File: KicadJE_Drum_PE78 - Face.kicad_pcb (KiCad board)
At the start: 2 copper layers, 183 x 128 mm, 212 parts, among them J101 Snare, J102 LCymbals, J103 SCymbals, J104 Maracas, J105 Bass, J106 LBongo, J107 HBongo, J108 Claves, J201 AudioJack2_SwitchT, J202 AudioJack2_SwitchT, J203 AudioJack2_SwitchT, J204 Power +, J205 Power -, J206 Conn_01x03_Male, J207 Conn_01x03_Male, J208 Conn_01x03_Male, J209 Conn_01x03_Male, J210 Conn_01x02_Male, J301 Tone/Noise, J302 RND, J303 Noise, J304 DRUM_OUT, J401 Tone/Noise, P101 HEADER_2x8_Doepfer, P201 HEADER_2x5_Doepfer, P401 HEADER_2x8_Doepfer, Q101 2N3904, Q102 2N3904, Q103 2N3904, Q104 2N3904, SW201 SW_SPDT, U101 74HC04, U302 TL072

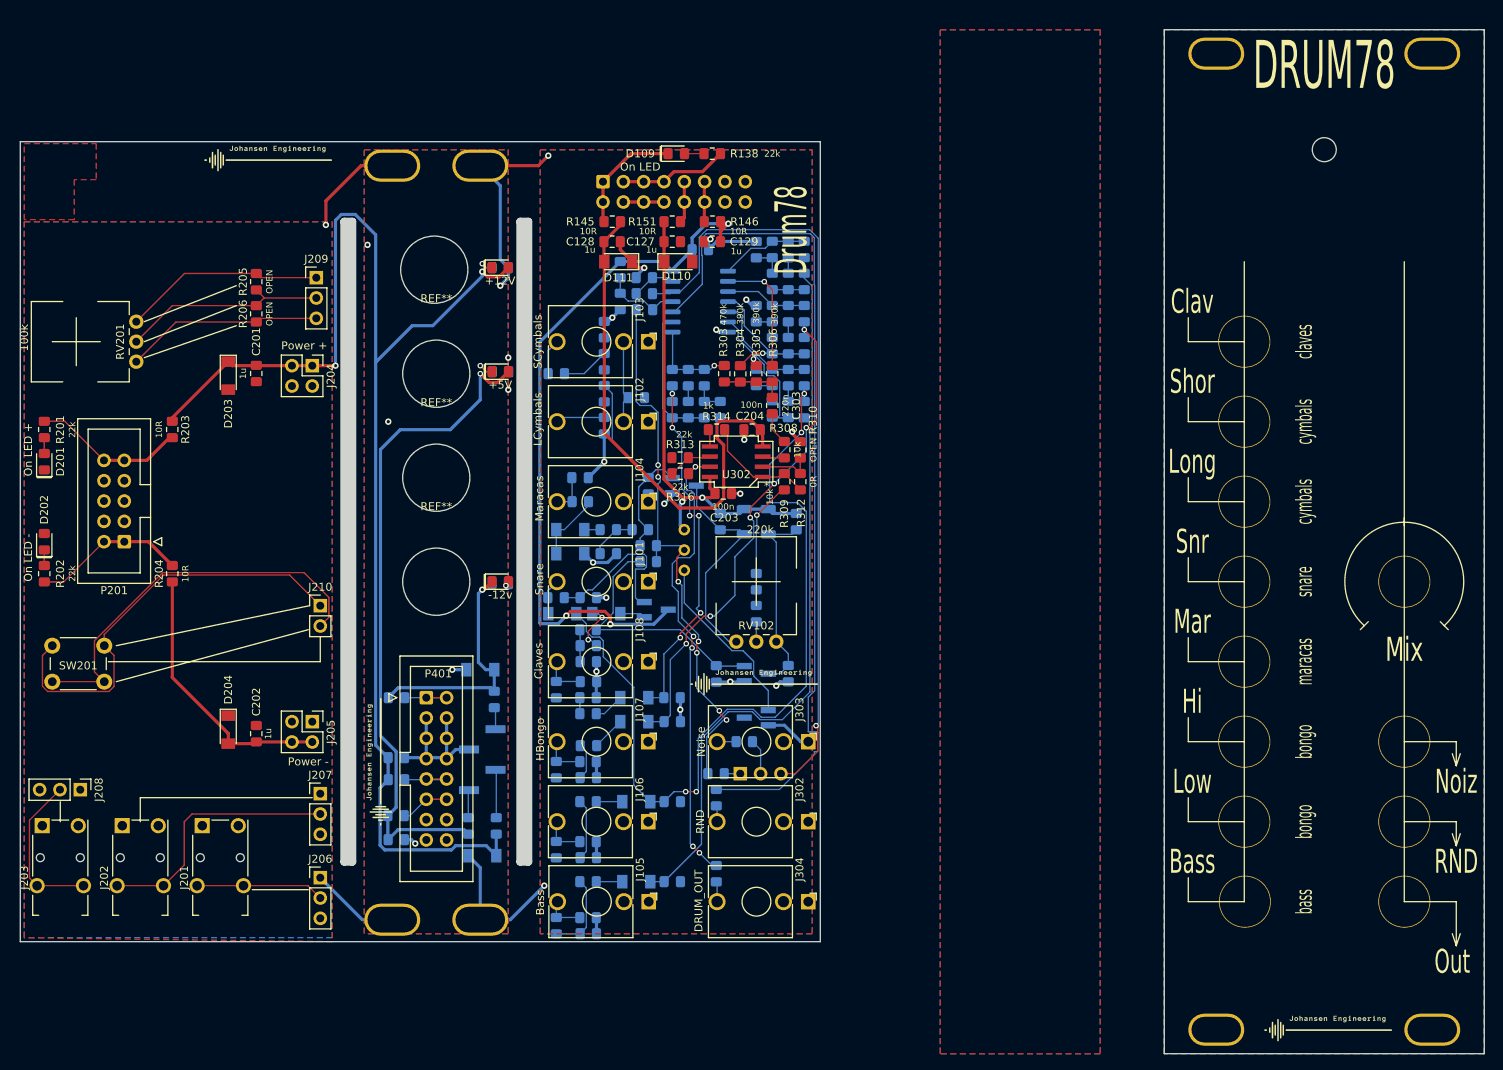
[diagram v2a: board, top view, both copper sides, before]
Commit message: base removed from face pcb
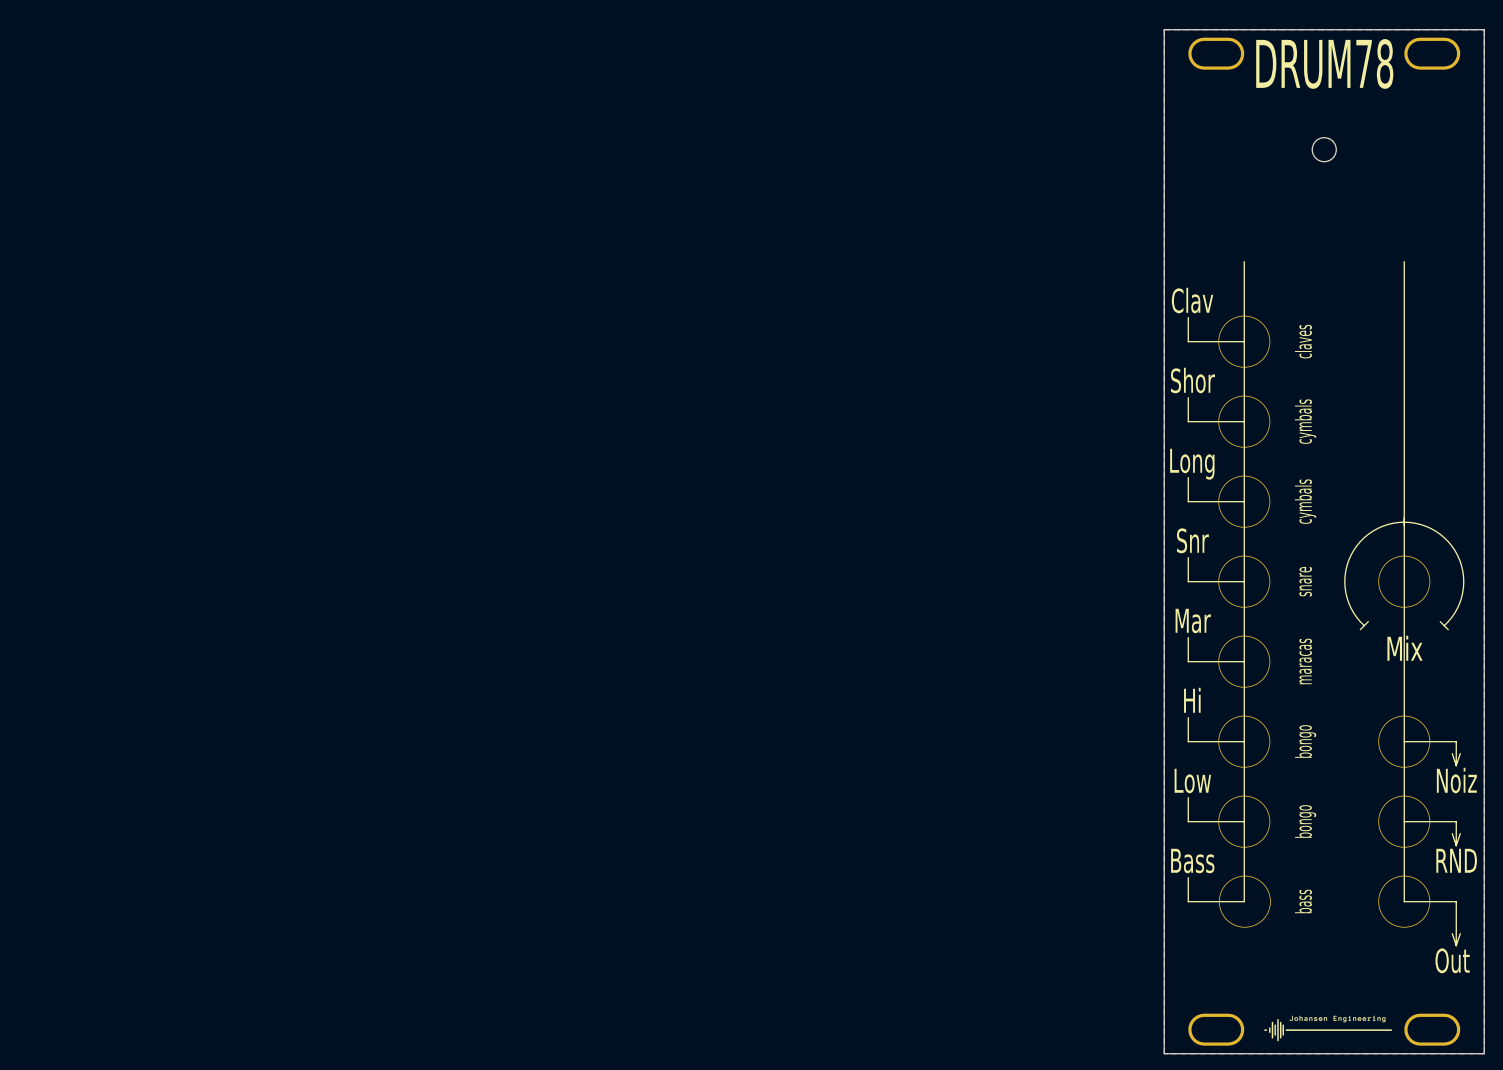
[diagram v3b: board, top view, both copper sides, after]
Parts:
- removed C101: 330n, AJ:C_0805_AJ
- removed C102, C107, C120, C130, C203, C204: 100n, AJ:C_0805_AJ
- removed C103, C303, C304: 220n, AJ:C_0805_AJ
- removed C104, C113: 150n, AJ:C_0805_AJ
- removed C105, C109, C114, C115: 47n, AJ:C_0805_AJ
- removed C106, C108: 68n, AJ:C_0805_AJ
- removed C110, C116: 15n, AJ:C_0805_AJ
- removed C111, C112, C119, C124, C301, C302: 4n7, AJ:C_0805_AJ
- removed C117: 22n, AJ:C_0805_AJ
- removed C118, C123: 33n, AJ:C_0805_AJ
- removed C121, C125: 10n, AJ:C_0805_AJ
- removed C122, C126: 1n5, AJ:C_0805_AJ
- removed C127, C128, C129, C201, C202, C401, C403: 1u, AJ:C_0805_AJ
- removed D101, D102, D103, D104, D105, D106, D107, D108: 1N4148, Diode_SMD:D_MiniMELF
- removed D109: On LED, AJ:D_0805_AJ
- removed D110, D111, D203, D204, D404, D405: 1N4007, Diode_SMD:D_MiniMELF
- removed D201: On LED +, AJ:D_0805_AJ
- removed D202: On LED -, AJ:D_0805_AJ
- removed D401: +12V, AJ:D_0805_AJ
- removed D402: +5V, AJ:D_0805_AJ
- removed D403: -12v, AJ:D_0805_AJ
- removed the G*** at (95.0, 127.5)
- removed the G*** at (141.8, 117.8)
- removed the G*** at (58.5, 52.2)
- removed the G*** at (87.5, 95.0)
- removed the G*** at (81.0, 52.2)
- removed the H103 at (107.5, 53.0)
- removed the H103 at (96.5, 53.0)
- removed the H103 at (107.5, 147.2)
- removed the H103 at (96.5, 147.2)
- removed J101: Snare, Connector_Audio:Jack_3.5mm_QingPu_WQP-PJ398SM_Vertical_CircularHoles
- removed J102: LCymbals, Connector_Audio:Jack_3.5mm_QingPu_WQP-PJ398SM_Vertical_CircularHoles
- removed J103: SCymbals, Connector_Audio:Jack_3.5mm_QingPu_WQP-PJ398SM_Vertical_CircularHoles
- removed J104: Maracas, Connector_Audio:Jack_3.5mm_QingPu_WQP-PJ398SM_Vertical_CircularHoles
- removed J105: Bass, Connector_Audio:Jack_3.5mm_QingPu_WQP-PJ398SM_Vertical_CircularHoles
- removed J106: LBongo, Connector_Audio:Jack_3.5mm_QingPu_WQP-PJ398SM_Vertical_CircularHoles
- removed J107: HBongo, Connector_Audio:Jack_3.5mm_QingPu_WQP-PJ398SM_Vertical_CircularHoles
- removed J108: Claves, Connector_Audio:Jack_3.5mm_QingPu_WQP-PJ398SM_Vertical_CircularHoles
- removed J201, J202, J203: AudioJack2_SwitchT, Connector_Audio:Jack_3.5mm_Switronic_ST-005-G_horizontal
- removed J204: Power +, Connector_PinHeader_2.54mm:PinHeader_2x02_P2.54mm_Vertical
- removed J205: Power -, Connector_PinHeader_2.54mm:PinHeader_2x02_P2.54mm_Vertical
- removed J206, J207, J208, J209: Conn_01x03_Male, Connector_PinHeader_2.54mm:PinHeader_1x03_P2.54mm_Vertical
- removed J210: Conn_01x02_Male, Connector_PinHeader_2.54mm:PinHeader_1x02_P2.54mm_Vertical
- removed J301: Tone/Noise, Connector_PinHeader_2.54mm:PinHeader_1x03_P2.54mm_Vertical
- removed J302: RND, Connector_Audio:Jack_3.5mm_QingPu_WQP-PJ398SM_Vertical_CircularHoles
- removed J303: Noise, Connector_Audio:Jack_3.5mm_QingPu_WQP-PJ398SM_Vertical_CircularHoles
- removed J304: DRUM_OUT, Connector_Audio:Jack_3.5mm_QingPu_WQP-PJ398SM_Vertical_CircularHoles
- removed J401: Tone/Noise, Connector_PinHeader_2.54mm:PinHeader_1x04_P2.54mm_Vertical_SMD_Pin1Left
- removed L103, L104: 100mH, Inductor_SMD:L_1206_3216Metric
- removed P101, P401: HEADER_2x8_Doepfer, Connector_IDC:IDC-Header_2x08_P2.54mm_Vertical
- removed P201: HEADER_2x5_Doepfer, Connector_IDC:IDC-Header_2x05_P2.54mm_Vertical
- removed Q101, Q102, Q103, Q104: 2N3904, Package_TO_SOT_SMD:SOT-23_Handsoldering
- removed R101, R103, R116, R117, R139, R140, R308, R309, R311, R405: 10k, AJ:R_0805_AJ
- removed R102, R106, R131, R138, R201, R202, R313, R316, R404, R406: 22k, AJ:R_0805_AJ
- removed R104, R105, R132, R133: 12k, AJ:R_0805_AJ
- removed R107, R108, R134, R135: 47k, AJ:R_0805_AJ
- removed R109, R110, R118, R123, R128: 1M, AJ:R_0805_AJ
- removed R111, R112, R136, R137: 27k, AJ:R_0805_AJ
- removed R113, R301, R302, R307: 100k, AJ:R_0805_AJ
- removed R114: 2k2, AJ:R_0805_AJ
- removed R115, R303: 470k, AJ:R_0805_AJ
- removed R119, R121, R141, R143: 150k, AJ:R_0805_AJ
- removed R120, R122, R125, R127, R142, R144, R148, R150: 68k, AJ:R_0805_AJ
- removed R124, R126, R147, R149: 0-470k, AJ:R_0805_AJ
- removed R129, R130: 4k7, AJ:R_0805_AJ
- removed R145, R146, R151, R203, R204, R407, R408, R409: 10R, AJ:R_0805_AJ
- removed R205, R206, R310: OPEN, AJ:R_0805_AJ
- removed R304, R305, R306: 390k, AJ:R_0805_AJ
- removed R312, R401, R402, R403: 0R, AJ:R_0805_AJ
- removed R314: 1k, AJ:R_0805_AJ
- removed R315: 470r, AJ:R_0805_AJ
- removed R323: 470R, AJ:R_0805_AJ
- removed REF** (x4): MountingHole_8.4mm_M8, MountingHole:MountingHole_8.4mm_M8
- removed RV101: R_POT_TRIM, Potentiometer_THT:Potentiometer_Bourns_3296W_Vertical
- removed RV102: 220k, AJ:Potentiometer_China_RK09_Single_Vertical_AJ
- removed RV201: 100k, AJ:Potentiometer_China_RK09_Single_Vertical_AJ
- removed SW201: SW_SPDT, Button_Switch_THT:SW_PUSH_6mm_H8mm
- removed U101: 74HC04, Package_SO:SO-14_5.3x10.2mm_P1.27mm
- removed U302: TL072, AJ:AJ_SO-8_5.3x6.2mm_P1.27mm
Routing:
- net +12Vc: track 226.4 -> 0.00 mm, vias 4 -> 0
- net +5V: track 174.3 -> 0.00 mm, vias 4 -> 0
- net GND: track 173.4 -> 0.00 mm, vias 24 -> 0
- net -12Vc: track 128.2 -> 0.00 mm, vias 1 -> 0
- net Net-(R323-Pad2): track 106.0 -> 0.00 mm
- net LBongoTrig: track 102.2 -> 0.00 mm, vias 4 -> 0
- net Net-(J301-Pad3): track 97.2 -> 0.00 mm, vias 1 -> 0
- net BassTrig: track 93.2 -> 0.00 mm
- net NoiseOut: track 69.8 -> 0.00 mm, vias 7 -> 0
- net HBongoTrig: track 62.8 -> 0.00 mm, vias 6 -> 0
- net Net-(R315-Pad2): track 60.2 -> 0.00 mm, vias 5 -> 0
- net Net-(J210-Pad1): track 53.7 -> 0.00 mm
- net Net-(J210-Pad2): track 50.2 -> 0.00 mm
- net ClavesTrig: track 46.2 -> 0.00 mm, vias 6 -> 0
- net Net-(J202-PadT): track 32.3 -> 0.00 mm
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- removed copper zone on F.Cu, net (none)
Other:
- board size 183 x 128 mm -> 40 x 128 mm
- board text removed: "BB-Power"
- board text removed: "Drum78"
- board text removed: "Drum78 - Rev A JE - 27/4-2021"
- board text removed: "KicadJE-BB-Power Johansen Engineering 22/4/2021 Rev A"
- board text removed: "KicadJE-PDU1 27/4/2021 Rev A"
- board text removed: "PDU1"

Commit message: Face tweaked
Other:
- board text added: "SQ Trig"
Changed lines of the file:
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@@
   (general
     (thickness 1.6)
-    (drawings 85)
+    (drawings 86)
     (tracks 0)
     (zones 0)
@@
   (page A4)
   (layers
-    (0 F.Cu signal)
-    (31 B.Cu signal)
+    (0 F.Cu signal hide)
+    (31 B.Cu signal hide)
     (32 B.Adhes user)
     (33 F.Adhes user)
@@
     (38 B.Mask user)
     (39 F.Mask user)
-    (40 Dwgs.User user)
+    (40 Dwgs.User user hide)
     (41 Cmts.User user)
     (42 Eco1.User user)
@@
       (xy 5.7912 -1.6002)) (layer F.SilkS) (width 0.01))
   )
+  (gr_text "SQ Trig" (at 203 61.5) (layer F.SilkS)
+    (effects (font (size 3 1.8) (thickness 0.45)))
+  )
   (gr_line (start 229.5 128) (end 230 126.5) (layer F.SilkS) (width 0.12))
   (gr_line (start 229.5 128) (end 229 126.5) (layer F.SilkS) (width 0.12))
@@
   (gr_line (start 229.5 150.5) (end 229.5 145) (layer F.SilkS) (width 0.12))
   (gr_line (start 203 145) (end 203 65) (layer F.SilkS) (width 0.12))
-  (gr_line (start 223 65) (end 223 145) (layer F.SilkS) (width 0.12))
+  (gr_line (start 223 125) (end 223 145) (layer F.SilkS) (width 0.12))
   (gr_line (start 66 51) (end -50 51) (layer Dwgs.User) (width 0.15))
   (zone (net 1) (net_name GND) (layer F.Cu) (hatch edge 0.508)
